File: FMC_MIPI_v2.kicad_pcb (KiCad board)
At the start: 6 copper layers, 69 x 112 mm, 138 parts, among them IC1 SN74AVC4T245PWR, IC2 AT24MAC402-MAHM-T, IC3 TCA9406DCUR, IC4 TCA9406DCUR, IC5 TCA9406DCUR, IC6 SN74AVC1T45DCKT, IC7 SN74AVC1T45DCKT, J1 ASP-134488-01, J2 QTH-060-01-L-D-A, U1 LP5907MFX-1.8, U2 SN74AVC2T45DCUR, U3 SN74AVCH16T245_DGV_48, U4 TLV75525PDBV, U5 TS3DDR3812_RUA_42, U6 TS3DDR3812_RUA_42, U7 LP5907MFX-1.2, U8 SN74AVCH16T245_DGV_48

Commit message: Finished initial placement
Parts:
- C1, C11, C12, C2, C25, C26, C27, C28, C29, C3, C30, C31, C32, C33, C34, C35, C36, C37, C38, C39, C40, C41, C5, C6, C7, C8, D3, D4, IC1, IC2, IC3, IC4, IC5, IC6, IC7, U1, U2, U4, U7: moved to B.Cu
- moved C6 156.9 mm to (102.9, 123.8)
- moved C31 155.8 mm to (125.3, 58.5), turned to 90 degrees
- moved D4 155.1 mm to (128.5, 62.1), turned to 0 degrees
- moved C26 153.7 mm to (128.8, 58.8), turned to 180 degrees
- moved C5 153.2 mm to (104.6, 123.8)
- moved U4 152.3 mm to (128.8, 55.1), turned to 270 degrees
- moved D3 150.5 mm to (132.6, 84.8), turned to 0 degrees
- moved C30 149.8 mm to (129.2, 83.7), turned to 90 degrees
- moved C25 148.8 mm to (128.5, 51.8), turned to 180 degrees
- moved C28 148.6 mm to (132.7, 82.7), turned to 180 degrees
- moved U7 146.7 mm to (132.6, 79.4), turned to 270 degrees
- moved D2 146.6 mm to (119.5, 136.5)
- moved C27 146.3 mm to (129.4, 75.5), turned to 270 degrees
- moved R17 146.1 mm to (129.2, 79.8)
- moved R16 145.9 mm to (132.1, 55.2), turned to 90 degrees
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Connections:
- C41 pad 2: (no net) -> /VOLT_1P8
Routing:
- net /LVDS_to_Jetson_lines/FMC_HS_CSI_C_D1_P: track 93.9 -> 88.9 mm
- net /LVDS_to_Jetson_lines/FMC_HS_CSI_C_D1_N: track 94.3 -> 89.2 mm
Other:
- board size 69 x 112 mm -> 69.3 x 111.8 mm

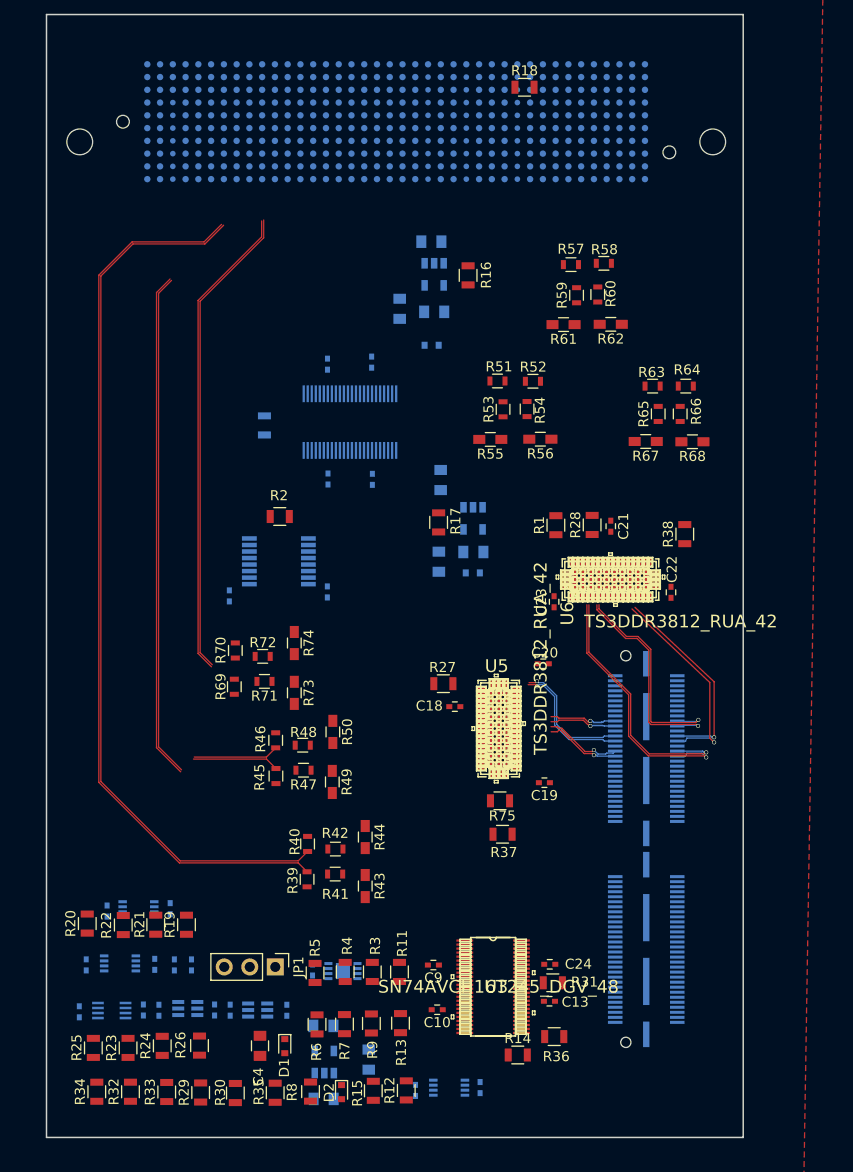
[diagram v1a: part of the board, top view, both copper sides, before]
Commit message: minor changes in positions
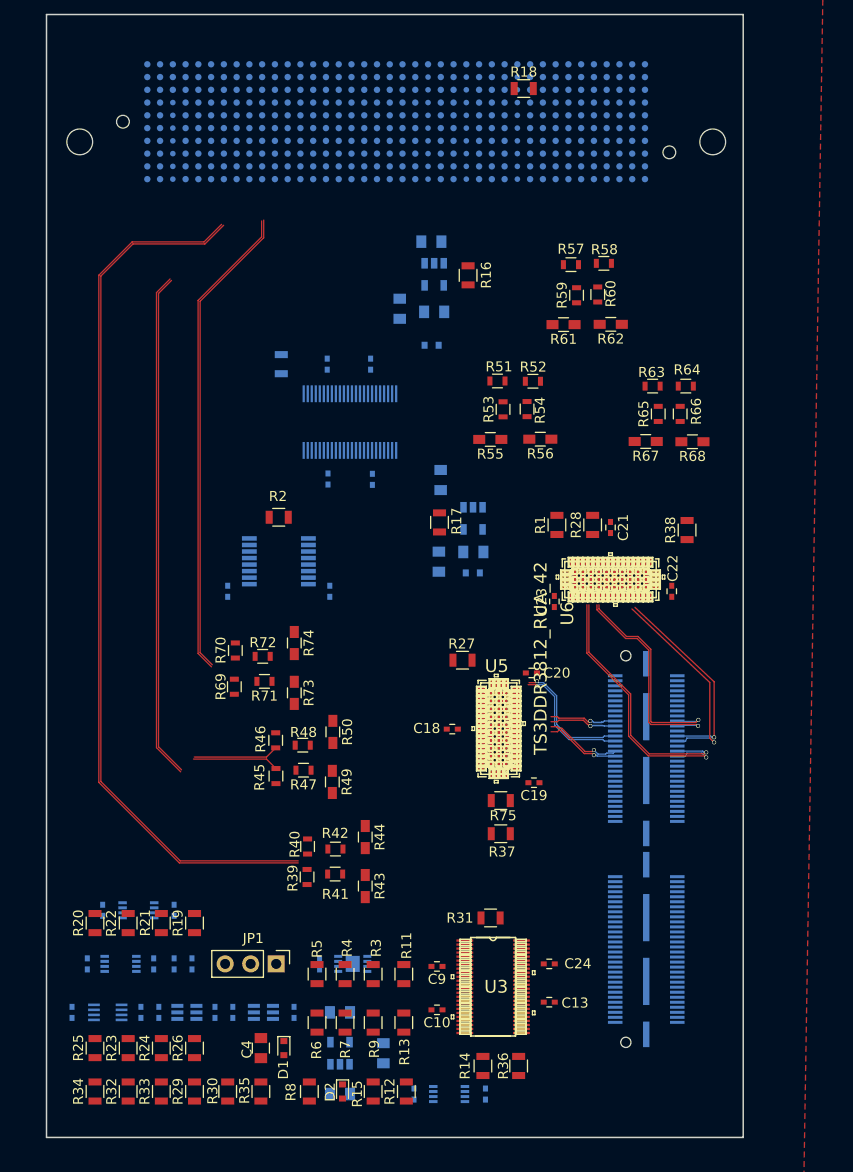
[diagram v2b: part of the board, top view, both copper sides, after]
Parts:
- moved R31 8.95 mm to (134.4, 119.1)
- moved R10 6.32 mm to (113.5, 64.0), turned to 90 degrees
- moved R36 4.59 mm to (137.2, 133.9), turned to 270 degrees
- moved R14 3.64 mm to (133.6, 133.9), turned to 90 degrees
- moved R27 3.01 mm to (131.6, 93.5)
- moved C18 2.25 mm to (130.6, 100.3)
- moved C8 2.13 mm to (119.4, 128.5)
- moved U1 1.79 mm to (119.4, 132.6)
- moved C7 1.70 mm to (119.4, 136.7)
- moved C29 1.59 mm to (123.7, 132.6)
- moved C20 1.50 mm to (138.4, 94.7)
- moved R35 1.43 mm to (111.5, 136.4)
- moved IC2 1.21 mm to (120.7, 123.7)
- moved C19 1.04 mm to (138.7, 105.7)
- moved C3 0.93 mm to (117.3, 123.7)
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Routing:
- net /LVDS_to_Jetson_lines/FMC_HS_CSI_C_D1_P: track 88.9 -> 87.5 mm
- net /LVDS_to_Jetson_lines/FMC_HS_CSI_C_D1_N: track 89.2 -> 88.0 mm

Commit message: placed nicely the components
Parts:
- R43, R44, R49, R50, R55, R56, R61, R62, R67, R68, R73, R74: footprint Resistors_SMD:R_0603_HandSoldering -> Resistors_SMD:R_0603
- moved R43 4.81 mm to (117.5, 114.0)
- moved R69 4.67 mm to (112.5, 93.2)
- moved R73 4.47 mm to (117.6, 93.2)
- moved R44 4.42 mm to (117.5, 111.0)
- moved R71 4.30 mm to (115.1, 92.7)
- moved R70 4.26 mm to (112.5, 90.2)
- moved R72 4.15 mm to (115.1, 90.7)
- moved R41 4.15 mm to (114.9, 113.5)
- moved R42 4.06 mm to (114.9, 111.5)
- moved R40 3.89 mm to (112.4, 111.0)
- moved R39 3.84 mm to (112.4, 114.0)
- moved C1 3.39 mm to (107.4, 83.3)
- moved C2 3.39 mm to (117.6, 83.3)
- moved IC1 3.39 mm to (112.5, 80.3)
- moved R2 3.24 mm to (112.6, 76.1)
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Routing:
- net /LVDS_to_Jetson_lines/FMC_HS_CSI_C_D1_N: track 88.0 -> 76.1 mm
- net /LVDS_to_Jetson_lines/FMC_HS_CSI_C_D1_P: track 87.5 -> 75.8 mm
- net /LVDS_to_Jetson_lines/FMC_HS_CSI_C_D0_N: track 59.2 -> 51.9 mm
- net /LVDS_to_Jetson_lines/FMC_HS_CSI_C_D0_P: track 58.7 -> 51.5 mm

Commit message: good, before FMC lines connect
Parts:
- moved C26 0.13 mm to (128.8, 58.9)
- moved C31 0.13 mm to (125.2, 58.4)
- moved D4 0.10 mm to (128.5, 62.2)
- moved R16 0.07 mm to (132.1, 55.1)
- moved U4 0.06 mm to (128.8, 55.1)
- moved C25 0.05 mm to (128.5, 51.8)
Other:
- net class Power added: clearance 0.1524, trace_width 0.254, via_dia 0.3556, via_drill 0.3048
- rule via_min_drill: 0.3 -> 0.127
- rule via_min_size: 0.4 -> 0.2032

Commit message: Added dummy nets to FMC connector
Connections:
- IC1 pad 4: (no net) -> FMC_SWITCH_DATA_LANES_VADJ
- IC1 pad 5: (no net) -> FMC_SWITCH_CLOCK_LANES_VADJ
- IC1 pad 6: (no net) -> FMC_EN_MIPI_OUT_DATA_VADJ
- IC1 pad 7: (no net) -> FMC_EN_MIPI_OUT_CLOCK_VADJ
- IC6 pad 4: (no net) -> FMC_1P2V_MONITOR
- IC7 pad 3: (no net) -> FMC_ENN_JT_GPIO_INPUT
- J1 pad A1: (no net) -> FMC_CAM0_PWR
- J1 pad A2: (no net) -> FMC_CAM0_RST
- J1 pad A3: (no net) -> FMC_CAM0_MCLK
- J1 pad A4: (no net) -> FMC_I2C2_CAM_CLK
- J1 pad A5: (no net) -> FMC_I2C2_CAM_DAT
- J1 pad A6: (no net) -> FMC_I2C3_CAM_CLK
- J1 pad A7: (no net) -> FMC_I2C3_CAM_DAT
- J1 pad B1: (no net) -> FMC_HS_CSI_C_D1_N
- J1 pad B10: (no net) -> FMC_HS_CSI_C_CLK_N
- J1 pad B11: (no net) -> FMC_HS_CSI_C_CLK_P
- J1 pad B12: (no net) -> FMC_HS_CSI_D_CLK_N
- J1 pad B13: (no net) -> FMC_LP_CSI_C_D1_P
- J1 pad B14: (no net) -> FMC_LP_CSI_C_D1_N
- J1 pad B15: (no net) -> FMC_LP_CSI_C_D0_N
- J1 pad B16: (no net) -> FMC_LP_CSI_C_D0_P
- J1 pad B17: (no net) -> FMC_LP_CSI_D_D1_N
- J1 pad B18: (no net) -> FMC_LP_CSI_D_D1_P
- J1 pad B19: (no net) -> FMC_LP_CSI_D_D0_P
- J1 pad B2: (no net) -> FMC_HS_CSI_C_D1_P
- J1 pad B20: (no net) -> FMC_LP_CSI_D_D0_N
- J1 pad B21: (no net) -> FMC_SWITCH_DATA_LANES_VADJ
- J1 pad B22: (no net) -> FMC_SWITCH_CLOCK_LANES_VADJ
- J1 pad B23: (no net) -> FMC_LP_CSI_C_CLK_P
- J1 pad B24: (no net) -> FMC_LP_CSI_C_CLK_N
- J1 pad B25: (no net) -> FMC_LP_CSI_D_CLK_P
- J1 pad B26: (no net) -> FMC_LP_CSI_D_CLK_N
- J1 pad B27: (no net) -> FMC_EN_MIPI_OUT_DATA_VADJ
- J1 pad B28: (no net) -> FMC_EN_MIPI_OUT_CLOCK_VADJ
- J1 pad B29: (no net) -> FMC_I2C_CAM_CLK
- J1 pad B3: (no net) -> FMC_HS_CSI_C_D0_N
- J1 pad B30: (no net) -> FMC_I2C_CAM_DAT
- J1 pad B31: (no net) -> FMC_GPIO17_OUT
- J1 pad B32: (no net) -> FMC_GPIO9_OUT
- J1 pad B33: (no net) -> FMC_ENN_JT_GPIO_INPUT
- J1 pad B34: (no net) -> FMC_1P8V_MONITOR
- J1 pad B35: (no net) -> FMC_3P3V_MONITOR
- J1 pad B36: (no net) -> FMC_2P8V_MONITOR
- J1 pad B37: (no net) -> FMC_1P2V_MONITOR
- J1 pad B4: (no net) -> FMC_HS_CSI_C_D0_P
- J1 pad B5: (no net) -> FMC_HS_CSI_D_D1_N
- J1 pad B6: (no net) -> FMC_HS_CSI_D_D1_P
- J1 pad B7: (no net) -> FMC_HS_CSI_D_D0_N
- J1 pad B8: (no net) -> FMC_HS_CSI_D_D0_P
- J1 pad B9: (no net) -> FMC_HS_CSI_D_CLK_P
- R14 pad 2: (no net) -> FMC_I2C_CAM_CLK
- R15 pad 2: (no net) -> FMC_I2C_CAM_DAT
- R21 pad 2: (no net) -> FMC_I2C2_CAM_CLK
- R22 pad 2: (no net) -> FMC_I2C2_CAM_DAT
- R25 pad 2: (no net) -> FMC_I2C3_CAM_CLK
- R26 pad 2: (no net) -> FMC_I2C3_CAM_DAT
- R39 pad 1: /LVDS_to_Jetson_lines/FMC_HS_CSI_C_D1_N -> FMC_HS_CSI_C_D1_N
- R40 pad 2: /LVDS_to_Jetson_lines/FMC_HS_CSI_C_D1_P -> FMC_HS_CSI_C_D1_P
- R41 pad 2: /LVDS_to_Jetson_lines/FMC_HS_CSI_C_D1_N -> FMC_HS_CSI_C_D1_N
- R42 pad 2: /LVDS_to_Jetson_lines/FMC_HS_CSI_C_D1_P -> FMC_HS_CSI_C_D1_P
- R45 pad 1: /LVDS_to_Jetson_lines/FMC_HS_CSI_C_D0_N -> FMC_HS_CSI_C_D0_N
- R46 pad 2: /LVDS_to_Jetson_lines/FMC_HS_CSI_C_D0_P -> FMC_HS_CSI_C_D0_P
- R47 pad 2: /LVDS_to_Jetson_lines/FMC_HS_CSI_C_D0_N -> FMC_HS_CSI_C_D0_N
- R48 pad 2: /LVDS_to_Jetson_lines/FMC_HS_CSI_C_D0_P -> FMC_HS_CSI_C_D0_P
- R51 pad 1: /LVDS_to_Jetson_lines/FMC_HS_CSI_D_D1_N -> FMC_HS_CSI_D_D1_N
- R52 pad 2: /LVDS_to_Jetson_lines/FMC_HS_CSI_D_D1_P -> FMC_HS_CSI_D_D1_P
- R53 pad 2: /LVDS_to_Jetson_lines/FMC_HS_CSI_D_D1_N -> FMC_HS_CSI_D_D1_N
- R54 pad 2: /LVDS_to_Jetson_lines/FMC_HS_CSI_D_D1_P -> FMC_HS_CSI_D_D1_P
- R57 pad 1: /LVDS_to_Jetson_lines/FMC_HS_CSI_D_D0_N -> FMC_HS_CSI_D_D0_N
- R58 pad 2: /LVDS_to_Jetson_lines/FMC_HS_CSI_D_D0_P -> FMC_HS_CSI_D_D0_P
- R59 pad 2: /LVDS_to_Jetson_lines/FMC_HS_CSI_D_D0_N -> FMC_HS_CSI_D_D0_N
- R60 pad 2: /LVDS_to_Jetson_lines/FMC_HS_CSI_D_D0_P -> FMC_HS_CSI_D_D0_P
- R63 pad 1: /LVDS_to_Jetson_lines/FMC_HS_CSI_D_CLK_N -> FMC_HS_CSI_D_CLK_N
- R64 pad 2: /LVDS_to_Jetson_lines/FMC_HS_CSI_D_CLK_P -> FMC_HS_CSI_D_CLK_P
- R65 pad 2: /LVDS_to_Jetson_lines/FMC_HS_CSI_D_CLK_N -> FMC_HS_CSI_D_CLK_N
- R66 pad 2: /LVDS_to_Jetson_lines/FMC_HS_CSI_D_CLK_P -> FMC_HS_CSI_D_CLK_P
- R69 pad 1: /LVDS_to_Jetson_lines/FMC_HS_CSI_C_CLK_N -> FMC_HS_CSI_C_CLK_N
- R70 pad 2: /LVDS_to_Jetson_lines/FMC_HS_CSI_C_CLK_P -> FMC_HS_CSI_C_CLK_P
- R71 pad 2: /LVDS_to_Jetson_lines/FMC_HS_CSI_C_CLK_N -> FMC_HS_CSI_C_CLK_N
- R72 pad 2: /LVDS_to_Jetson_lines/FMC_HS_CSI_C_CLK_P -> FMC_HS_CSI_C_CLK_P
- U2 pad 6: (no net) -> FMC_3P3V_MONITOR
- U2 pad 7: (no net) -> FMC_2P8V_MONITOR
- U3 pad 19: (no net) -> FMC_GPIO9_OUT
- U3 pad 2: (no net) -> FMC_CAM0_MCLK
- U3 pad 20: (no net) -> FMC_GPIO17_OUT
- U3 pad 5: (no net) -> FMC_CAM0_PWR
- U3 pad 6: (no net) -> FMC_CAM0_RST
- U3 pad 8: (no net) -> FMC_1P8V_MONITOR
- U8 pad 16: (no net) -> FMC_LP_CSI_C_D0_N
- U8 pad 17: (no net) -> FMC_LP_CSI_C_D0_P
- U8 pad 19: (no net) -> FMC_LP_CSI_D_D1_N
- U8 pad 2: (no net) -> FMC_LP_CSI_D_CLK_N
- U8 pad 20: (no net) -> FMC_LP_CSI_D_D1_P
- U8 pad 22: (no net) -> FMC_LP_CSI_D_D0_N
- U8 pad 23: (no net) -> FMC_LP_CSI_D_D0_P
- U8 pad 3: (no net) -> FMC_LP_CSI_D_CLK_P
- U8 pad 5: (no net) -> FMC_LP_CSI_C_CLK_N
- U8 pad 6: (no net) -> FMC_LP_CSI_C_CLK_P
- U8 pad 8: (no net) -> FMC_LP_CSI_C_D1_N
- U8 pad 9: (no net) -> FMC_LP_CSI_C_D1_P

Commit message: started routing
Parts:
- C10, C13, C24, C9: moved to B.Cu
- C14, C15, C16, C17: moved to F.Cu
- moved R57 11.0 mm to (142.2, 66.8)
- moved R58 11.0 mm to (145.3, 66.8)
- moved R61 11.0 mm to (142.2, 71.9)
- moved R62 11.0 mm to (145.3, 71.9)
- moved R59 11.0 mm to (142.7, 69.3)
- moved R60 11.0 mm to (144.8, 69.3)
- moved R25 6.60 mm to (101.6, 132.1)
- moved R16 5.40 mm to (128.5, 51.1), turned to 0 degrees
- moved C14 4.90 mm to (122.9, 66.8), turned to 0 degrees
- moved C17 4.89 mm to (122.9, 68.8), turned to 0 degrees
- moved C13 4.89 mm to (135.9, 129.8), turned to 270 degrees
- moved C10 4.82 mm to (133.6, 129.8), turned to 270 degrees
- moved C9 4.67 mm to (133.3, 122.2), turned to 90 degrees
- moved C24 4.58 mm to (135.9, 122.2), turned to 90 degrees
- moved C16 4.44 mm to (115.8, 69.3), turned to 180 degrees
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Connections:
- J1 pad A1: FMC_CAM0_PWR -> (no net)
- J1 pad A2: FMC_CAM0_RST -> (no net)
- J1 pad A3: FMC_CAM0_MCLK -> (no net)
- J1 pad A4: FMC_I2C2_CAM_CLK -> (no net)
- J1 pad A5: FMC_I2C2_CAM_DAT -> (no net)
- J1 pad A6: FMC_I2C3_CAM_CLK -> (no net)
- J1 pad A7: FMC_I2C3_CAM_DAT -> (no net)
- J1 pad B1: FMC_HS_CSI_C_D1_N -> (no net)
- J1 pad B10: FMC_HS_CSI_C_CLK_N -> (no net)
- J1 pad B11: FMC_HS_CSI_C_CLK_P -> (no net)
- J1 pad B12: FMC_HS_CSI_D_CLK_N -> (no net)
- J1 pad B13: FMC_LP_CSI_C_D1_P -> (no net)
- J1 pad B14: FMC_LP_CSI_C_D1_N -> (no net)
- J1 pad B15: FMC_LP_CSI_C_D0_N -> (no net)
- J1 pad B16: FMC_LP_CSI_C_D0_P -> (no net)
- J1 pad B17: FMC_LP_CSI_D_D1_N -> (no net)
- J1 pad B18: FMC_LP_CSI_D_D1_P -> (no net)
- J1 pad B19: FMC_LP_CSI_D_D0_P -> (no net)
- J1 pad B2: FMC_HS_CSI_C_D1_P -> (no net)
- J1 pad B20: FMC_LP_CSI_D_D0_N -> (no net)
- J1 pad B21: FMC_SWITCH_DATA_LANES_VADJ -> (no net)
- J1 pad B22: FMC_SWITCH_CLOCK_LANES_VADJ -> (no net)
- J1 pad B23: FMC_LP_CSI_C_CLK_P -> (no net)
- J1 pad B24: FMC_LP_CSI_C_CLK_N -> (no net)
- J1 pad B25: FMC_LP_CSI_D_CLK_P -> (no net)
- J1 pad B26: FMC_LP_CSI_D_CLK_N -> (no net)
- J1 pad B27: FMC_EN_MIPI_OUT_DATA_VADJ -> (no net)
- J1 pad B28: FMC_EN_MIPI_OUT_CLOCK_VADJ -> (no net)
- J1 pad B29: FMC_I2C_CAM_CLK -> (no net)
- J1 pad B3: FMC_HS_CSI_C_D0_N -> (no net)
- J1 pad B30: FMC_I2C_CAM_DAT -> (no net)
- J1 pad B31: FMC_GPIO17_OUT -> (no net)
- J1 pad B32: FMC_GPIO9_OUT -> (no net)
- J1 pad B33: FMC_ENN_JT_GPIO_INPUT -> (no net)
- J1 pad B34: FMC_1P8V_MONITOR -> (no net)
- J1 pad B35: FMC_3P3V_MONITOR -> (no net)
- J1 pad B36: FMC_2P8V_MONITOR -> (no net)
- J1 pad B37: FMC_1P2V_MONITOR -> (no net)
- J1 pad B4: FMC_HS_CSI_C_D0_P -> (no net)
- J1 pad B5: FMC_HS_CSI_D_D1_N -> (no net)
- J1 pad B6: FMC_HS_CSI_D_D1_P -> (no net)
- J1 pad B7: FMC_HS_CSI_D_D0_N -> (no net)
- J1 pad B8: FMC_HS_CSI_D_D0_P -> (no net)
- J1 pad B9: FMC_HS_CSI_D_CLK_P -> (no net)
- J1 pad D11: (no net) -> FMC_I2C2_CAM_DAT
- J1 pad D14: (no net) -> FMC_EN_MIPI_OUT_DATA_VADJ
- J1 pad D15: (no net) -> FMC_EN_MIPI_OUT_CLOCK_VADJ
- J1 pad D17: (no net) -> FMC_ENN_JT_GPIO_INPUT
- J1 pad D26: (no net) -> FMC_GPIO17_OUT
- J1 pad D27: (no net) -> FMC_GPIO9_OUT
- J1 pad D8: (no net) -> FMC_2P8V_MONITOR
- J1 pad D9: (no net) -> FMC_3P3V_MONITOR
- J1 pad G10: (no net) -> FMC_I2C3_CAM_DAT
- J1 pad G12: (no net) -> FMC_SWITCH_DATA_LANES_VADJ
- J1 pad G13: (no net) -> FMC_SWITCH_CLOCK_LANES_VADJ
- J1 pad G15: (no net) -> FMC_LP_CSI_D_D1_P
- J1 pad G16: (no net) -> FMC_LP_CSI_D_D1_N
- J1 pad G18: (no net) -> FMC_LP_CSI_D_D0_P
- J1 pad G19: (no net) -> FMC_LP_CSI_D_D0_N
- J1 pad G21: (no net) -> FMC_LP_CSI_D_CLK_P
- J1 pad G22: (no net) -> FMC_LP_CSI_D_CLK_N
- J1 pad G24: (no net) -> FMC_I2C_CAM_DAT
- J1 pad G25: (no net) -> FMC_I2C_CAM_CLK
- J1 pad G27: (no net) -> FMC_1P8V_MONITOR
- J1 pad G28: (no net) -> FMC_CAM0_RST
- J1 pad G30: (no net) -> FMC_CAM0_PWR
- J1 pad G33: (no net) -> FMC_CAM0_MCLK
- J1 pad G6: (no net) -> FMC_HS_CSI_C_CLK_P
- J1 pad G7: (no net) -> FMC_HS_CSI_C_CLK_N
- J1 pad G9: (no net) -> FMC_I2C2_CAM_CLK
- J1 pad H10: (no net) -> FMC_HS_CSI_C_D1_P
- J1 pad H11: (no net) -> FMC_HS_CSI_C_D1_N
- J1 pad H13: (no net) -> FMC_HS_CSI_C_D0_P
- J1 pad H14: (no net) -> FMC_HS_CSI_C_D0_N
- J1 pad H16: (no net) -> FMC_LP_CSI_C_D1_P
- J1 pad H17: (no net) -> FMC_LP_CSI_C_D1_N
- J1 pad H19: (no net) -> FMC_LP_CSI_C_D0_P
- J1 pad H20: (no net) -> FMC_LP_CSI_C_D0_N
- J1 pad H22: (no net) -> FMC_LP_CSI_C_CLK_P
- J1 pad H23: (no net) -> FMC_LP_CSI_C_CLK_N
- J1 pad H31: (no net) -> FMC_HS_CSI_D_D1_P
- J1 pad H32: (no net) -> FMC_HS_CSI_D_D1_N
- J1 pad H34: (no net) -> FMC_HS_CSI_D_D0_P
- J1 pad H35: (no net) -> FMC_HS_CSI_D_D0_N
- J1 pad H37: (no net) -> FMC_HS_CSI_D_CLK_P
- J1 pad H38: (no net) -> FMC_HS_CSI_D_CLK_N
- J1 pad H7: (no net) -> FMC_I2C3_CAM_CLK
- J1 pad H8: (no net) -> FMC_1P2V_MONITOR
- U8 pad 16: FMC_LP_CSI_C_D0_N -> FMC_LP_CSI_D_D1_N
- U8 pad 17: FMC_LP_CSI_C_D0_P -> FMC_LP_CSI_D_D1_P
- U8 pad 19: FMC_LP_CSI_D_D1_N -> FMC_LP_CSI_D_D0_N
- U8 pad 2: FMC_LP_CSI_D_CLK_N -> FMC_LP_CSI_C_D1_N
- U8 pad 20: FMC_LP_CSI_D_D1_P -> FMC_LP_CSI_D_D0_P
- U8 pad 22: FMC_LP_CSI_D_D0_N -> FMC_LP_CSI_D_CLK_N
- U8 pad 23: FMC_LP_CSI_D_D0_P -> FMC_LP_CSI_D_CLK_P
- U8 pad 26: /LVDS_to_Jetson_lines/LP_CSI_D_D0_P -> /LVDS_to_Jetson_lines/LP_CSI_D_CLK_P
- U8 pad 27: /LVDS_to_Jetson_lines/LP_CSI_D_D0_N -> /LVDS_to_Jetson_lines/LP_CSI_D_CLK_N
- U8 pad 29: /LVDS_to_Jetson_lines/LP_CSI_D_D1_P -> /LVDS_to_Jetson_lines/LP_CSI_D_D0_P
- U8 pad 3: FMC_LP_CSI_D_CLK_P -> FMC_LP_CSI_C_D1_P
- U8 pad 30: /LVDS_to_Jetson_lines/LP_CSI_D_D1_N -> /LVDS_to_Jetson_lines/LP_CSI_D_D0_N
- U8 pad 32: /LVDS_to_Jetson_lines/LP_CSI_C_D0_P -> /LVDS_to_Jetson_lines/LP_CSI_D_D1_P
- U8 pad 33: /LVDS_to_Jetson_lines/LP_CSI_C_D0_N -> /LVDS_to_Jetson_lines/LP_CSI_D_D1_N
- U8 pad 40: /LVDS_to_Jetson_lines/LP_CSI_C_D1_P -> /LVDS_to_Jetson_lines/LP_CSI_C_CLK_P
- U8 pad 41: /LVDS_to_Jetson_lines/LP_CSI_C_D1_N -> /LVDS_to_Jetson_lines/LP_CSI_C_CLK_N
- U8 pad 43: /LVDS_to_Jetson_lines/LP_CSI_C_CLK_P -> /LVDS_to_Jetson_lines/LP_CSI_C_D0_P
- U8 pad 44: /LVDS_to_Jetson_lines/LP_CSI_C_CLK_N -> /LVDS_to_Jetson_lines/LP_CSI_C_D0_N
- U8 pad 46: /LVDS_to_Jetson_lines/LP_CSI_D_CLK_P -> /LVDS_to_Jetson_lines/LP_CSI_C_D1_P
- U8 pad 47: /LVDS_to_Jetson_lines/LP_CSI_D_CLK_N -> /LVDS_to_Jetson_lines/LP_CSI_C_D1_N
- U8 pad 5: FMC_LP_CSI_C_CLK_N -> FMC_LP_CSI_C_D0_N
- U8 pad 6: FMC_LP_CSI_C_CLK_P -> FMC_LP_CSI_C_D0_P
- U8 pad 8: FMC_LP_CSI_C_D1_N -> FMC_LP_CSI_C_CLK_N
- U8 pad 9: FMC_LP_CSI_C_D1_P -> FMC_LP_CSI_C_CLK_P
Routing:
- net FMC_GPIO17_OUT: track 0.00 -> 117.4 mm, vias 0 -> 2
- net FMC_GPIO9_OUT: track 0.00 -> 112.7 mm, vias 0 -> 2
- net FMC_2P8V_MONITOR: track 0.00 -> 109.5 mm
- net FMC_3P3V_MONITOR: track 0.00 -> 105.4 mm
- net FMC_I2C3_CAM_CLK: track 0.00 -> 104.6 mm, vias 0 -> 1
- net FMC_ENN_JT_GPIO_INPUT: track 0.00 -> 103.0 mm, vias 0 -> 3
- net FMC_1P8V_MONITOR: track 0.00 -> 102.0 mm, vias 0 -> 2
- net FMC_I2C_CAM_CLK: track 0.00 -> 101.5 mm, vias 0 -> 1
- net FMC_I2C3_CAM_DAT: track 0.00 -> 100.8 mm, vias 0 -> 2
- net FMC_CAM0_RST: track 0.00 -> 99.3 mm, vias 0 -> 2
- net FMC_I2C2_CAM_DAT: track 0.00 -> 97.7 mm, vias 0 -> 1
- net FMC_CAM0_PWR: track 0.00 -> 97.6 mm, vias 0 -> 2
- net FMC_CAM0_MCLK: track 0.00 -> 95.3 mm, vias 0 -> 2
- net FMC_1P2V_MONITOR: track 0.00 -> 93.8 mm, vias 0 -> 3
- net FMC_I2C_CAM_DAT: track 0.00 -> 92.4 mm, vias 0 -> 1
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
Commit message: before hi-speed routing
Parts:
- added JP2: Jumper, Pin_Headers:Pin_Header_Straight_1x02_Pitch2.54mm, F.Cu at (112.0, 58.7)
- added JP3: Jumper, Pin_Headers:Pin_Header_Straight_1x02_Pitch2.54mm, F.Cu at (128.5, 67.6)
- C18, C20, C21, C22, C23: moved to B.Cu
- C27, C37, C38, C41: moved to F.Cu
- moved R37 20.0 mm to (140.7, 91.4), turned to 90 degrees
- moved R75 16.1 mm to (137.2, 91.4), turned to 90 degrees
- moved R28 13.0 mm to (133.9, 87.4), turned to 270 degrees
- moved R1 8.29 mm to (137.2, 87.4), turned to 270 degrees
- moved R10 6.07 mm to (111.3, 68.0), turned to 270 degrees
- moved R26 3.30 mm to (108.2, 132.1)
- moved C27 3.16 mm to (132.3, 76.7), turned to 180 degrees
- moved R27 3.06 mm to (133.9, 91.4), turned to 90 degrees
- moved C20 2.75 mm to (136.9, 97.0), turned to 90 degrees
- moved C41 2.55 mm to (112.3, 128.8), turned to 0 degrees
- moved C2 2.27 mm to (115.6, 84.3)
- moved C18 2.18 mm to (132.3, 99.1), turned to 270 degrees
- moved C19 1.37 mm to (137.4, 106.2), turned to 90 degrees
- moved R17 1.27 mm to (128.0, 79.8)
- moved C21 1.08 mm to (147.1, 81.0)
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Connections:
- R39 pad 2: /VOLT_2P5 -> /LVDS_to_Jetson_lines/VOLT_2P5_CSI_C
- R40 pad 1: /VOLT_2P5 -> /LVDS_to_Jetson_lines/VOLT_2P5_CSI_C
- R45 pad 2: /VOLT_2P5 -> /LVDS_to_Jetson_lines/VOLT_2P5_CSI_C
- R46 pad 1: /VOLT_2P5 -> /LVDS_to_Jetson_lines/VOLT_2P5_CSI_C
- R51 pad 2: /VOLT_2P5 -> /LVDS_to_Jetson_lines/VOLT_2P5_CSI_D
- R52 pad 1: /VOLT_2P5 -> /LVDS_to_Jetson_lines/VOLT_2P5_CSI_D
- R57 pad 2: /VOLT_2P5 -> /LVDS_to_Jetson_lines/VOLT_2P5_CSI_D
- R58 pad 1: /VOLT_2P5 -> /LVDS_to_Jetson_lines/VOLT_2P5_CSI_D
- R63 pad 2: /VOLT_2P5 -> /LVDS_to_Jetson_lines/VOLT_2P5_CSI_D
- R64 pad 1: /VOLT_2P5 -> /LVDS_to_Jetson_lines/VOLT_2P5_CSI_D
- R69 pad 2: /VOLT_2P5 -> /LVDS_to_Jetson_lines/VOLT_2P5_CSI_C
- R70 pad 1: /VOLT_2P5 -> /LVDS_to_Jetson_lines/VOLT_2P5_CSI_C
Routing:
- net /VDD_VADJ: track 7.58 -> 325.7 mm, vias 3 -> 17
- net /VOLT_3P3: track 0.00 -> 314.8 mm, vias 0 -> 17
- net /VOLT_1P8: track 5.12 -> 130.3 mm, vias 2 -> 11
- net /VOLT_1P2: track 2.35 -> 93.8 mm, vias 1 -> 4
- net /Jetson_connector/JT_VDD_2V8: track 0.00 -> 87.9 mm, vias 0 -> 3
- net JT_VDD_1V8: track 0.00 -> 79.2 mm, vias 0 -> 4
- net /Jetson_connector/JT_VDD_3V3: track 0.00 -> 76.4 mm, vias 0 -> 2
- net /LVDS_to_Jetson_lines/EN_MIPI_OUT_CSI_C: track 0.00 -> 59.2 mm, vias 0 -> 4
- net /Jetson_connector/JT_VDD_1V2: track 0.00 -> 59.1 mm, vias 0 -> 3
- net /LVDS_to_Jetson_lines/EN_MIPI_OUT_CSI_D: track 0.00 -> 47.5 mm, vias 0 -> 3
- net JT_1p8V_I2C2_CAM_CLK: track 0.00 -> 46.7 mm, vias 0 -> 1
- net Earth: track 0.97 -> 39.6 mm, vias 2 -> 26
- net /LVDS_to_Jetson_lines/SWITCH_DATA_LANES_CSI_CD: track 0.00 -> 30.4 mm, vias 0 -> 1
- net /LVDS_to_Jetson_lines/SWITCH_CLOCK_LANES_CSI_CD: track 0.00 -> 25.2 mm, vias 0 -> 1
- net Net-(R33-Pad2): track 0.00 -> 21.7 mm, vias 0 -> 2
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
